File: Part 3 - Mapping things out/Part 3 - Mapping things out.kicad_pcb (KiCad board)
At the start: 2 copper layers, 100 x 100.1 mm, 83 parts, among them J1 BUS 1, J2 EXT BUS, SW1 RESET, SW2 MODE, SW3 SPEED, SW4 BOOT SPEED, SW5 BOOT MODE, SW6 STEP, SW7 RESET FAST, U1 74AHC14, U10 LMC555, U11 74AHC138, U12 74HC251, U13 74HC251, U2 74AHC174, U3 74AHC08, U4 74AHC14, U5 74AHC74, U6 74AHC74, U7 74AHC74, U8 74AHC74, U9 74AHC74, X1 14.7456MHz

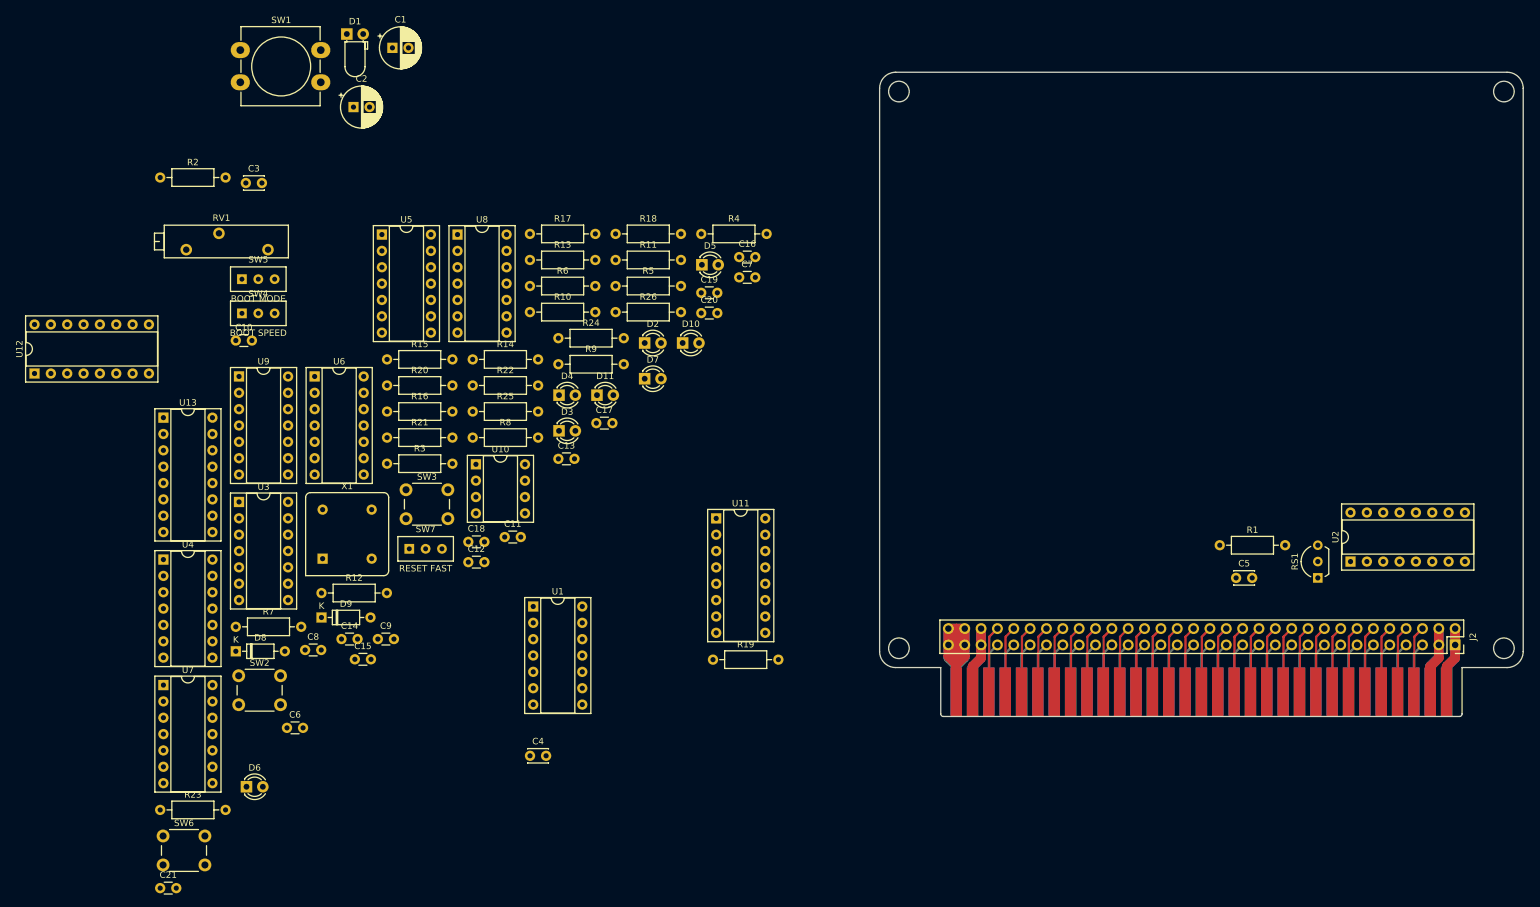
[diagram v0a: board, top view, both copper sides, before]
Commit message: Updated clock, and created CPU card
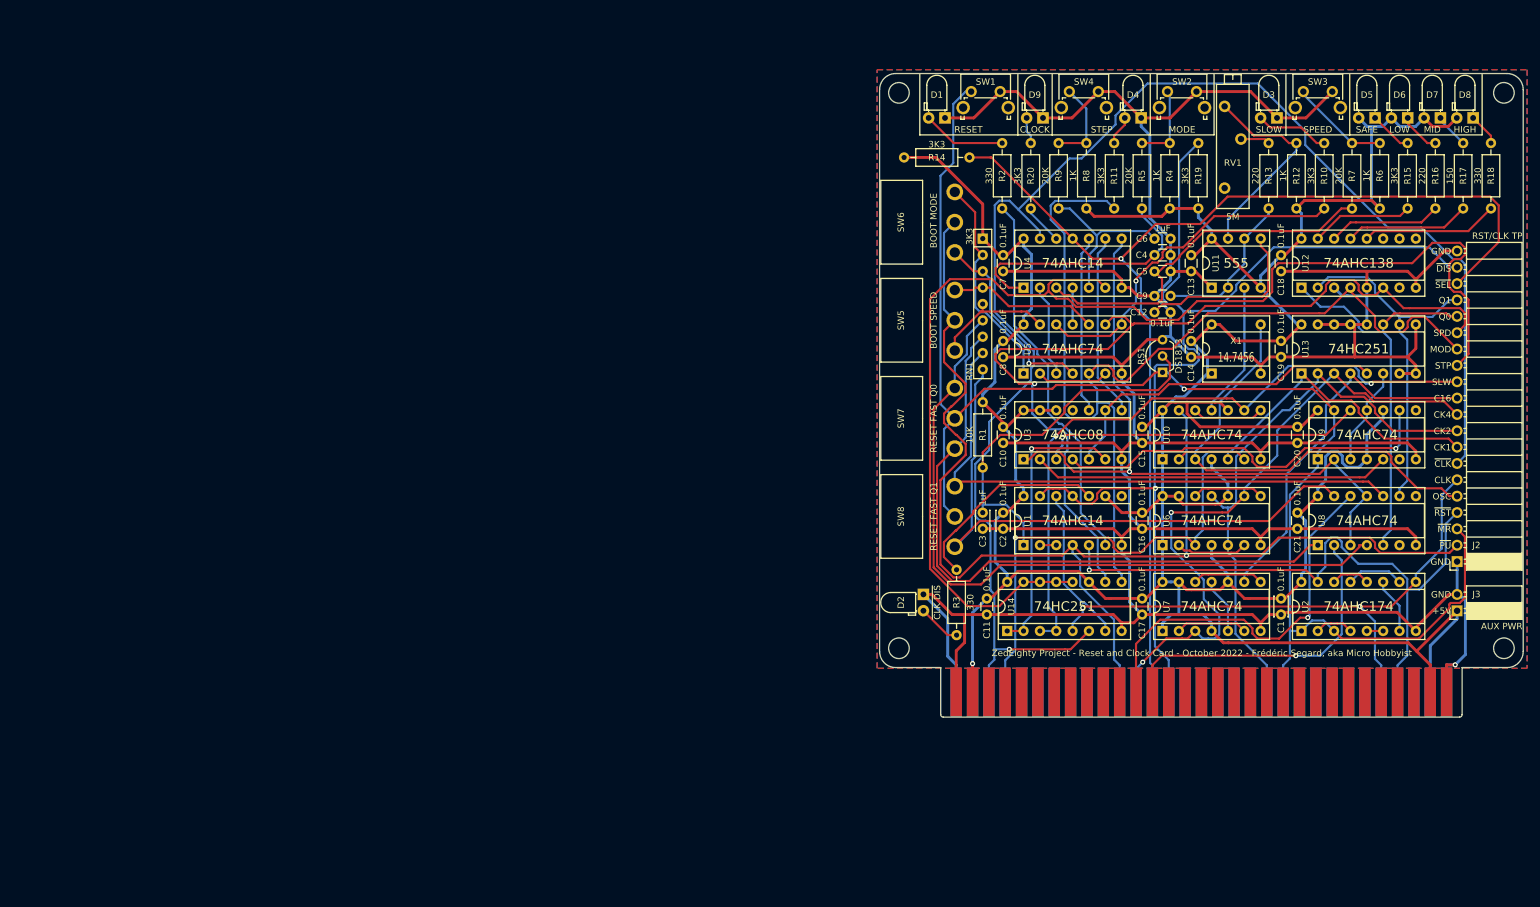
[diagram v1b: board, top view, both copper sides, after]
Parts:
- removed the C1 at (13.7, 42.1)
- removed the C2 at (7.64, 51.3)
- removed the D3 at (39.6, 101.6)
- removed the D4 at (39.6, 96.1)
- removed the D9 at (2.67, 130.6)
- removed the R10 at (35.1, 83.2)
- removed the R11 at (48.4, 75.1)
- removed the R12 at (2.67, 126.8)
- removed the R13 at (35.1, 75.1)
- removed R22, R24: 3K3, Resistor_THT:R_Axial_DIN0207_L6.3mm_D2.5mm_P10.16mm_Horizontal
- removed the R7 at (-10.6, 132.1)
- removed the R8 at (26.2, 102.7)
- added C20: 0.1uF, Capacitor_THT:C_Disc_D3.0mm_W1.6mm_P2.50mm, F.Cu at (154.3, 101.0)
- added C21: 0.1uF, Capacitor_THT:C_Disc_D3.0mm_W1.6mm_P2.50mm, F.Cu at (154.3, 114.3)
- added D2: ~{CLK DIS}, LED_THT:LED_D3.0mm_Horizontal_O1.27mm_Z2.0mm_Clear, F.Cu at (96.2, 127.0)
- added J3: AUX PWR, Connector_PinSocket_2.54mm:PinSocket_1x02_P2.54mm_Horizontal, F.Cu at (179.1, 129.6)
- added R18: 330, Resistor_THT:R_Axial_DIN0207_L6.3mm_D2.5mm_P10.16mm_Horizontal, F.Cu at (184.4, 67.1)
- added R3: 330, Resistor_THT:R_Axial_DIN0207_L6.3mm_D2.5mm_P10.16mm_Horizontal, F.Cu at (101.3, 123.2)
- added RN1: 3K3, Resistor_THT:R_Array_SIP9, F.Cu at (105.4, 71.7)
- added SW8: RESET FAST Q1, 0_Z80_Library:Microswitch_4.7mm_spacing, F.Cu at (101.1, 114.9)
- added U10: 74AHC74, Package_DIP:DIP-14_W7.62mm_Socket, F.Cu at (133.3, 106.0)
- C1: renamed from C3; value 1uF -> 0.1uF
- C2: renamed from C4; value 1uF -> 0.1uF
- C9: renamed from C8; value 0.10uF -> 0.1uF
- D1: value RST LED -> RESET
- D3: renamed from D2; footprint LED_THT:LED_D3.0mm -> LED_THT:LED_D3.0mm_Horizontal_O1.27mm_Z2.0mm_Clear
- D4: renamed from D5; footprint LED_THT:LED_D3.0mm -> LED_THT:LED_D3.0mm_Horizontal_O1.27mm_Z2.0mm_Clear
- D5: renamed from D6; value LOW -> SAFE; footprint LED_THT:LED_D3.0mm -> LED_THT:LED_D3.0mm_Horizontal_O1.27mm_Z2.0mm_Clear
- D6: renamed from D7; value MID -> LOW; footprint LED_THT:LED_D3.0mm -> LED_THT:LED_D3.0mm_Horizontal_O1.27mm_Z2.0mm_Clear
- D7: renamed from D10; value HIGH -> MID; footprint LED_THT:LED_D3.0mm -> LED_THT:LED_D3.0mm_Horizontal_O1.27mm_Z2.0mm_Clear
- D8: value 1N4148 -> HIGH; footprint Diode_THT:D_DO-35_SOD27_P7.62mm_Horizontal -> LED_THT:LED_D3.0mm_Horizontal_O1.27mm_Z2.0mm_Clear
- D9: renamed from D11; footprint LED_THT:LED_D3.0mm -> LED_THT:LED_D3.0mm_Horizontal_O1.27mm_Z2.0mm_Clear
- J2: value EXT BUS -> RST/CLK TP; footprint Connector_PinSocket_2.54mm:PinSocket_2x32_P2.54mm_Vertical -> Connector_PinSocket_2.54mm:PinSocket_1x20_P2.54mm_Horizontal
- R10: renamed from R9; value 150 -> 3K3
- R15: renamed from R23; value 330 -> 3K3
- SW1: footprint Button_Switch_THT:SW_PUSH-12mm_Wuerth-430476085716 -> Button_Switch_THT:SW_Tactile_SPST_Angled_PTS645Vx58-2LFS
- SW2, SW3: footprint Button_Switch_THT:SW_PUSH_6mm -> Button_Switch_THT:SW_Tactile_SPST_Angled_PTS645Vx58-2LFS
- SW4: renamed from SW6; footprint Button_Switch_THT:SW_PUSH_6mm -> Button_Switch_THT:SW_Tactile_SPST_Angled_PTS645Vx58-2LFS
- SW5: renamed from SW4; footprint 0_Z80_Library:Microswitch_2.54mm_spacing -> 0_Z80_Library:Microswitch_4.7mm_spacing
- SW6: renamed from SW5; footprint 0_Z80_Library:Microswitch_2.54mm_spacing -> 0_Z80_Library:Microswitch_4.7mm_spacing
- SW7: value RESET FAST -> RESET FAST Q0; footprint 0_Z80_Library:Microswitch_2.54mm_spacing -> 0_Z80_Library:Microswitch_4.7mm_spacing
- X1: footprint Oscillator:Oscillator_DIP-8 -> 0_Z80_Library:DIP-8-4_W7.62mm_Oscillator_Socket
- moved R15 215.2 mm to (171.4, 67.1), turned to 90 degrees
- moved D8 209.4 mm to (181.6, 53.0), turned to 180 degrees
- moved D5 203.8 mm to (166.4, 53.0), turned to 180 degrees
- moved U13 196.9 mm to (154.9, 92.7)
- moved SW4 182.2 mm to (118.9, 48.9)
- moved C14 181.3 mm to (137.8, 87.7), turned to -90 degrees
- moved C1 173.3 mm to (151.8, 127.7), turned to -90 degrees
- moved R17 171.0 mm to (180.1, 67.1), turned to 90 degrees
- moved SW2 170.5 mm to (134.1, 48.9)
- moved U9 168.1 mm to (157.5, 106.0), turned to 90 degrees
- moved R16 165.2 mm to (175.7, 67.1), turned to 90 degrees
- moved U7 155.5 mm to (133.3, 132.7), turned to 90 degrees
- moved C4 153.5 mm to (132.1, 74.3)
- moved SW3 152.5 mm to (155.2, 48.9)
- moved RV1 148.9 mm to (143.0, 63.9), turned to -90 degrees
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- renumbered C15 to C10, C17 to C11, C10 to C12, C19 to C13, C21 to C14, C12 to C15, C14 to C16, C16 to C17, C20 to C19, C5 to C3, C6 to C4, C7 to C5, C9 to C6, C11 to C7, C13 to C8, R14 to R11, R15 to R12, R16 to R13, R19 to R14, R20 to R16, R21 to R17, R25 to R19, R26 to R20, R3 to R4, R4 to R5, R5 to R6, R6 to R7, R17 to R8, R18 to R9, U10 to U11, U11 to U12, U12 to U13, U13 to U14
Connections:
- net Net-(R11-Pad1) renamed /Clock/R12
- net Net-(R12-Pad1) renamed /Clock/R13
- net Net-(R22-Pad1) renamed /Clock/R20
- net Net-(R24-Pad1) renamed /Clock/R24
- net Net-(R7-Pad1) renamed /Clock/R9
- net Net-(R8-Pad1) renamed /Clock/R10
- D5 pad 1: Net-(D6-Pad1) -> Net-(D5-Pad1)
- D6 pad 1: Net-(D7-Pad1) -> Net-(D6-Pad1)
- D7 pad 1: Net-(D10-Pad1) -> Net-(D7-Pad1)
- D8 pad 2: Net-(D8-Pad2) -> +5V
- J1 pad 49: /~{CLK_EN} -> /~{CLK_DIS}
- J1 pad 59: /USER7 -> /CLK1
- J1 pad 60: /USER8 -> /~{CLK}
- J2 pad 10: /A13 -> /CLK4
- J2 pad 11: /~{INT} -> /CLK16
- J2 pad 12: /A12 -> /SLOW
- J2 pad 13: /~{MREQ} -> /STEP
- J2 pad 14: /A11 -> /MODE
- J2 pad 15: /~{WR} -> /SPEED
- J2 pad 16: /A10 -> /Q0
- J2 pad 17: /~{RD} -> /Q1
- J2 pad 18: /A9 -> /~{CLK_SEL}
- J2 pad 19: /~{IORQ} -> /~{CLK_DIS}
- J2 pad 2: GND -> /~{PWR_UP}
- J2 pad 20: /A8 -> GND
- J2 pad 3: +5V -> /~{MR}
- J2 pad 4: +5V -> /~{RESET}
- J2 pad 5: /~{M1} -> /OSC
- J2 pad 6: /A15 -> /CLK
- J2 pad 7: /~{RESET} -> /~{CLK}
- J2 pad 8: /A14 -> /CLK1
- J2 pad 9: /CLK -> /CLK2
- R11 pad 1: /Clock/MODE -> /MODE
- R15 pad 1: Net-(D8-Pad2) -> Net-(R15-Pad1)
- R15 pad 2: Net-(D10-Pad1) -> Net-(D5-Pad1)
- R16 pad 1: Net-(R20-Pad1) (its old number) -> Net-(R16-Pad1)
- R17 pad 1: Net-(R21-Pad1) -> Net-(R17-Pad1)
- R19 pad 1: /~{CLK_EN} -> /~{CLK_DIS}
- U1 pad 10: unconnected-(U1-Pad10) -> Net-(R3-Pad1)
- U1 pad 11: +5V -> /~{CLK_DIS}
- U1 pad 13: /~{CLK_EN} -> /~{CLK_DIS}
- U11 pad 3: Net-(U10-Pad3) -> Net-(U10-Pad11)
- U12 pad 1: /Clock/Q0 -> /Q0
- U12 pad 13: Net-(D8-Pad1) -> Net-(R17-Pad1)
- U12 pad 14: Net-(R21-Pad1) -> Net-(R16-Pad1)
- U12 pad 15: Net-(R20-Pad1) (its old number) -> Net-(R15-Pad1)
- U12 pad 2: /Clock/Q1 -> /Q1
- U12 pad 4: /Clock/MODE -> /MODE
- U12 pad 6: /Clock/SPEED -> /SPEED
- U13 pad 1: /Clock/CLK1 -> /CLK1
- U13 pad 10: /Clock/Q1 -> /Q1
- U13 pad 11: /Clock/Q0 -> /Q0
- U13 pad 2: /Clock/CLK1 -> /CLK2
- U13 pad 3: /CLK2 -> /CLK4
- U13 pad 4: /CLK4 -> /CLK16
- U13 pad 5: Net-(U12-Pad5) -> /Clock/Yout
- U14 pad 10: /Clock/SPEED -> /SPEED
- U14 pad 12: /Clock/STEP -> /STEP
- U14 pad 13: /Clock/STEP -> /STEP
- U14 pad 14: /Clock/STEP -> /STEP
- U14 pad 15: /Clock/STEP -> /STEP
- U14 pad 3: /Clock/SLOW -> /SLOW
- U14 pad 4: /Clock/SLOW -> /SLOW
- U14 pad 6: Net-(U13-Pad6) (its old number) -> /~{CLK}
- U14 pad 9: /Clock/MODE -> /MODE
- U3 pad 5: Net-(U12-Pad5) -> /Clock/Yout
- U3 pad 9: /Clock/CLK1 -> /Clock/Yout
- U4 pad 13: Net-(U13-Pad6) (its old number) -> /~{CLK}
- U4 pad 6: /Clock/STEP -> /STEP
- U5 pad 5: /Clock/MODE -> /MODE
- U5 pad 9: /Clock/SPEED -> /SPEED
- U6 pad 3: /Clock/CLK1 -> /CLK1
- U7 pad 11: Net-(U10-Pad3) -> Net-(U7-Pad11)
- U7 pad 13: /~{PWR_UP} -> +5V
- U7 pad 3: Net-(U7-Pad3) -> /CLK4
- U7 pad 5: /Clock/CLK1 -> Net-(U7-Pad11)
- U7 pad 9: /Clock/SLOW -> /CLK16
- U8 pad 10: +5V -> /Clock/R25
- U8 pad 13: /~{MR} -> /Clock/R21
- U8 pad 5: /Clock/Q0 -> /Q0
- U8 pad 9: /Clock/Q1 -> /Q1
- X1 pad 5: Net-(U7-Pad3) -> /OSC
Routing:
- net GND: track 77.1 -> 614.3 mm, vias 0 -> 1
- net +5V: track 41.7 -> 545.6 mm, vias 0 -> 1
- net /~{CLK}: track 0.00 -> 233.1 mm, vias 0 -> 1
- net /~{MR}: track 7.88 -> 225.5 mm, vias 0 -> 1
- net /STEP: track 0.00 -> 196.0 mm
- net /~{PWR_UP}: track 7.88 -> 197.2 mm, vias 0 -> 1
- net /~{CLK_SEL}: track 7.88 -> 177.5 mm, vias 0 -> 1
- net /~{CLK_DIS}: track 0.00 -> 167.6 mm, vias 0 -> 1
- net /MODE: track 0.00 -> 160.4 mm
- net /SPEED: track 0.00 -> 136.3 mm, vias 0 -> 1
- net /CLK1: track 0.00 -> 121.6 mm, vias 0 -> 1
- net /Clock/R20: track 0.00 -> 112.7 mm
- net Net-(U3-Pad1): track 0.00 -> 105.8 mm, vias 0 -> 1
- net /SLOW: track 0.00 -> 104.0 mm, vias 0 -> 2
- net /Clock/R24: track 0.00 -> 101.0 mm
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- added copper zone on B.Cu, net GND
- added copper zone on F.Cu, net GND
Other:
- board size 100 x 100.1 mm -> 100 x 100 mm
- board text added: "+5V"
- board text added: "-- SLOW --"
- board text added: "--- RESET ---"
- board text added: "---- STEP ----"
- board text added: "------ FAST ------"
- board text added: "0.4608"
- board text added: "1.8432"
- board text added: "1.8M"
- board text added: "14.7456"
- board text added: "3.6864"
- board text added: "3.6M"
- board text added: "460K"
- board text added: "555"
- board text added: "7.3728"
- board text added: "7.4M"
- board text added: "< MODE >"
- board text added: "< SPEED >"
- board text added: "BOOT MODE"
- board text added: "BOOT SPEED"
- board text added: "C16"
- board text added: "CK1"
- board text added: "CK2"
- board text added: "CK4"
- board text added: "CLK"
- board text added: "CLK DIS"
- board text added: "CLOCK"
- board text added: "FAST"
- board text added: "FREE RUN"
- board text added: "GND"
- board text added: "JLCJLCJLCJLC"
- board text added: "MOD"
- board text added: "MODE"
- board text added: "OSC"
- board text added: "Q0"
- board text added: "Q0:0"
- board text added: "Q0:1"
- board text added: "Q1"
- board text added: "Q1:0"
- board text added: "Q1:1"
- board text added: "RESET FAST 0"
- board text added: "RESET FAST 1"
- board text added: "SINGLE STEP"
- board text added: "SLOW"
- board text added: "SLW"
- board text added: "SPD"
- board text added: "SPEED"
- board text added: "STEP"
- board text added: "STP"
- board text added: "ZedEighty Project - Reset and Clock Card - October 2022 - Frédéric Segard, aka Micro Hobbyist"
- board text added: "~{CLK_DIS}"
- board text added: "~{CLK_SEL}"
- board text added: "~{CLK}"
- board text added: "~{DIS}"
- board text added: "~{MR}"
- board text added: "~{PU}"
- board text added: "~{PWR_UP}"
- board text added: "~{RESET}"
- board text added: "~{RST}"
- board text added: "~{SEL}"
